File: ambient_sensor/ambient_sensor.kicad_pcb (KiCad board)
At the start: 2 copper layers, 69.5 x 54 mm, 29 parts, among them J1 Conn_01x02_Pin, J3 Conn_01x05_Pin, J4 Conn_01x01_Pin, J5 Conn_01x04_Pin, J6 Conn_01x02_Pin, U4 ATmega328-P, U6 LD1117S33TR_SOT223, Y1 Crystal

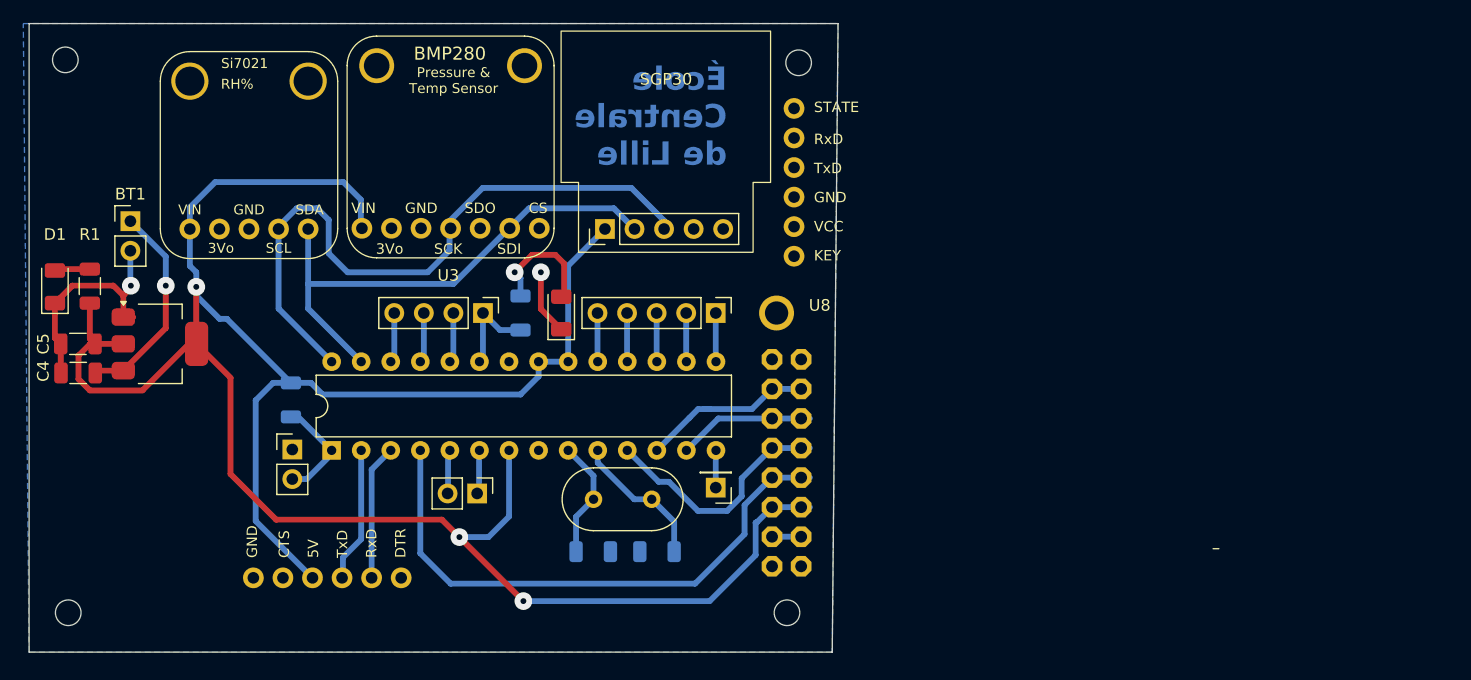
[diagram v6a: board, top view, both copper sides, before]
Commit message: fixing schematics
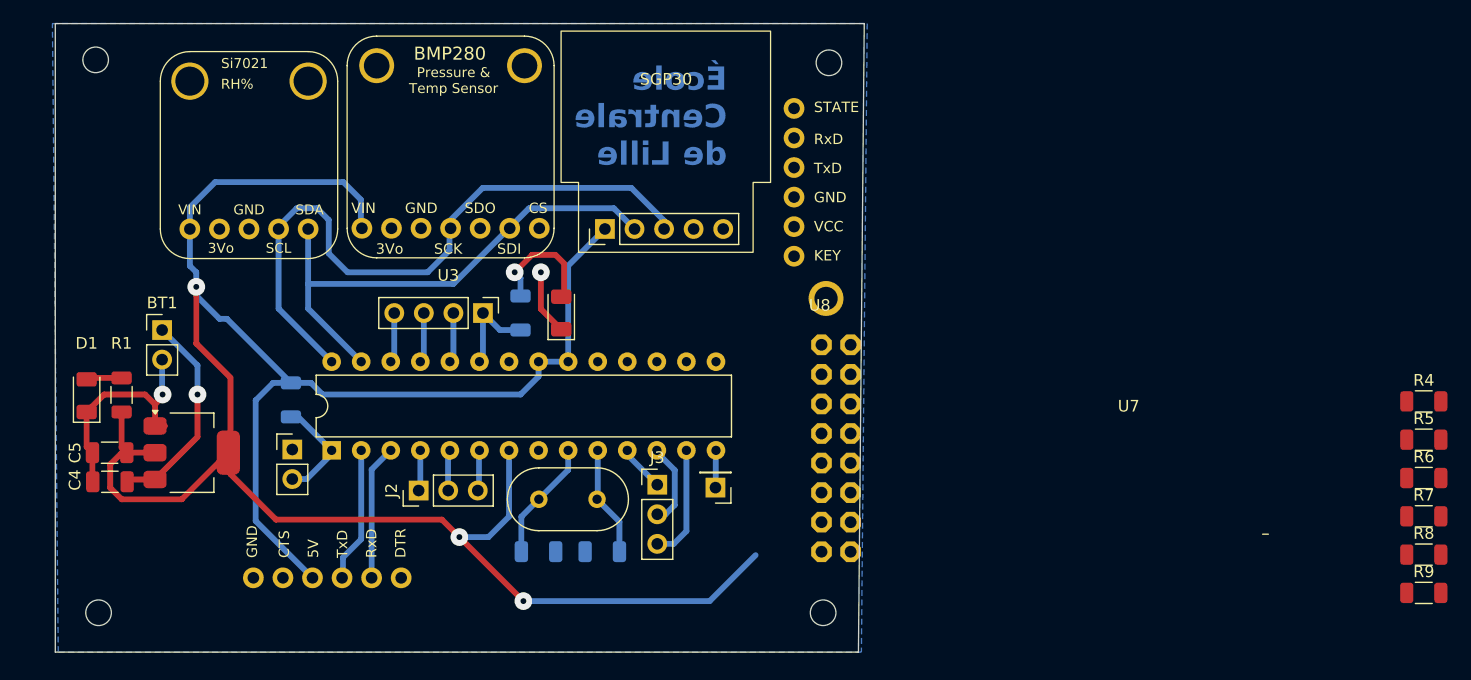
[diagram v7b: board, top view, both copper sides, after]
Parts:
- removed J6: Conn_01x02_Pin, Connector_PinHeader_2.54mm:PinHeader_1x02_P2.54mm_Vertical
- added J2: Conn_01x03_Pin, Connector_PinHeader_2.54mm:PinHeader_1x03_P2.54mm_Vertical, F.Cu at (196.2, 131.2)
- added R4: 1.8K, Resistor_SMD:R_1206_3216Metric, F.Cu at (282.6, 123.6)
- added R5: 1.0K, Resistor_SMD:R_1206_3216Metric, F.Cu at (282.6, 126.9)
- added R6: 1.8K, Resistor_SMD:R_1206_3216Metric, F.Cu at (282.6, 130.2)
- added R7: 3.3K, Resistor_SMD:R_1206_3216Metric, F.Cu at (282.6, 133.5)
- added R8: 3.3K, Resistor_SMD:R_1206_3216Metric, F.Cu at (282.6, 136.8)
- added R9: 2.2K, Resistor_SMD:R_1206_3216Metric, F.Cu at (282.6, 140.0)
- J3: value Conn_01x05_Pin -> Conn_01x03_Pin; footprint Connector_PinHeader_2.54mm:PinHeader_1x05_P2.54mm_Vertical -> Connector_PinHeader_2.54mm:PinHeader_1x03_P2.54mm_Vertical
- moved J3 15.6 mm to (216.8, 130.8), turned to 0 degrees
- moved BT1 9.74 mm to (174.2, 117.5)
- moved C4 9.74 mm to (169.7, 130.5)
- moved C5 9.74 mm to (169.7, 128.0)
- moved D1 9.74 mm to (167.7, 123.1)
- moved R1 9.74 mm to (170.7, 123.0)
- moved U6 9.74 mm to (176.8, 128.0)
- moved REF** 4.75 mm to (111.0, 145.8)
- moved Y1 4.70 mm to (211.6, 132.0)
- moved C1 4.70 mm to (206.6, 136.5)
- moved C2 4.70 mm to (212.0, 136.5)
- moved U7 4.43 mm to (275.2, 140.5)
- moved REF** 3.10 mm to (231.0, 141.8)
- moved REF** 2.60 mm to (168.5, 94.2)
- moved REF** 2.60 mm to (168.8, 141.8)
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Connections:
- net RST renamed /RST
- net SCL renamed /SCL
- net SDA renamed /SDA
- C2 pad 1: /CS -> Net-(U4-XTAL2/PB7)
- J3 pad 1: /RxS -> Net-(J3-Pin_1)
- U4 pad 10: /CS -> Net-(U4-XTAL2/PB7)
- U4 pad 11: /MOSI -> Net-(J3-Pin_1)
- U4 pad 12: /MISO -> Net-(J3-Pin_2)
- U4 pad 13: unconnected-(U4-PD7-Pad13) -> Net-(J3-Pin_3)
- U4 pad 16: Net-(J3-Pin_2) -> /CS
- U4 pad 17: Net-(J3-Pin_3) -> /MOSI
- U4 pad 18: Net-(J3-Pin_4) -> /MISO
- U4 pad 4: /DT -> Net-(J2-Pin_1)
- U7 pad 4: /DT -> Net-(U7-CS)
- U7 pad 5: /MOSI -> Net-(U7-MOSI)
- U7 pad 6: /CLK -> Net-(U7-SCK)
- Y1 pad 1: /CS -> Net-(U4-XTAL2/PB7)
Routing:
- net /DT: track 47.9 -> 0.00 mm
- net /MOSI: track 20.8 -> 0.03 mm
- net /CLK: track 15.9 -> 0.03 mm
- net /MISO: track 15.1 -> 0.03 mm
- net /CS: track 12.3 -> 0.03 mm
- net Net-(U4-XTAL2/PB7): track 0.00 -> 9.52 mm
- net +5V: track 207.6 -> 200.3 mm
- net Net-(J3-Pin_3): track 4.19 -> 9.90 mm
- net Net-(J3-Pin_1): track 0.00 -> 4.62 mm
- net Net-(J3-Pin_4): track 4.19 -> 0.00 mm
- net /RxS: track 4.19 -> 0.03 mm
- net Net-(J2-Pin_1): track 0.00 -> 3.51 mm
- net Net-(J3-Pin_2): track 4.19 -> 7.16 mm
- net unconnected-(U7-3V3-Pad2)_1 (its old number): track 2.50 -> 0.00 mm

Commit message: no warnings, I need a switch
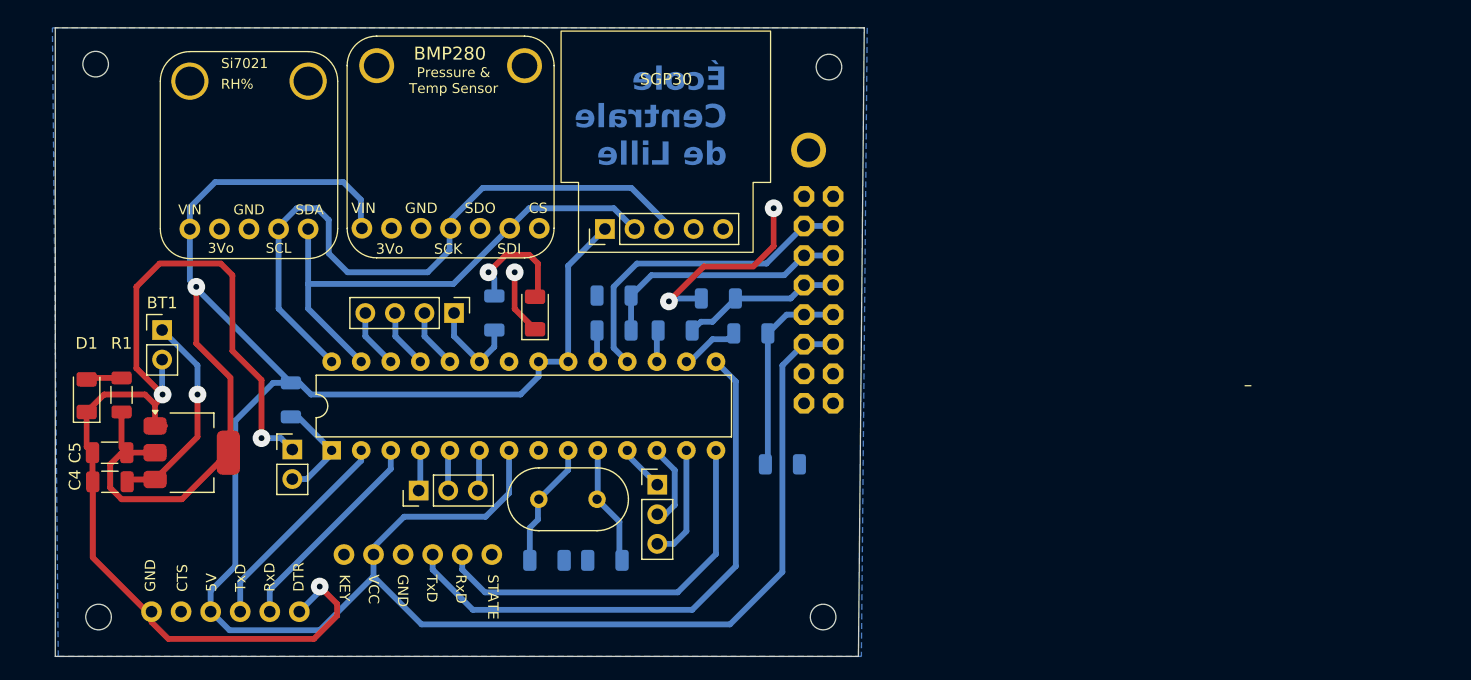
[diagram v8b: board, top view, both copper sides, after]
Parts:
- removed J4: Conn_01x01_Pin, Connector_PinHeader_2.54mm:PinHeader_1x01_P2.54mm_Vertical
- R4, R5, R6, R7, R8, R9: moved to B.Cu
- moved R8 73.0 mm to (213.0, 114.5), turned to 180 degrees
- moved R6 70.7 mm to (213.0, 117.5)
- moved R9 65.7 mm to (222.0, 114.8), turned to 180 degrees
- moved R5 65.0 mm to (218.3, 117.5)
- moved R4 58.1 mm to (224.8, 117.8)
- moved R7 55.3 mm to (227.5, 129.0)
- moved U8 51.1 mm to (185.1, 139.0), turned to -90 degrees
- moved U7 12.8 mm to (273.8, 127.8)
- moved U5 9.22 mm to (191.0, 141.7)
- moved J5 2.49 mm to (199.3, 116.0)
- moved D2 2.25 mm to (206.2, 116.0)
- moved R3 2.25 mm to (202.8, 116.0)
- moved C1 1.04 mm to (207.3, 137.2)
- moved C2 0.78 mm to (212.2, 137.2)
- moved REF** 0.37 mm to (168.5, 94.6)
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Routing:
- net GND: track 26.1 -> 118.7 mm, vias 2 -> 6
- net /RxS: track 0.03 -> 48.6 mm
- net +5V: track 200.3 -> 236.6 mm, vias 3 -> 1
- net /TxS: track 3.21 -> 34.2 mm
- net /MISO: track 0.03 -> 27.9 mm
- net Net-(U7-SCK): track 0.00 -> 21.8 mm
- net Net-(U7-CS): track 0.00 -> 17.6 mm
- net Net-(U7-MOSI): track 0.00 -> 13.7 mm
- net /TX: track 11.6 -> 18.2 mm
- net /RX: track 11.6 -> 18.2 mm
- net /CS: track 0.03 -> 5.10 mm
- net /MOSI: track 0.03 -> 2.75 mm
- net /CLK: track 0.03 -> 2.70 mm
- net Net-(J5-Pin_2): track 3.80 -> 5.51 mm
- net Net-(J5-Pin_3): track 3.80 -> 5.51 mm
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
